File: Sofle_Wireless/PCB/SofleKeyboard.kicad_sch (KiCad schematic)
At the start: 121 parts, among them J1 Conn_01x05, SW1 SW1, SW10 SW10, SW11 SW11, SW12 SW12, SW13 SW13, SW14 SW14, SW15 SW15, SW16 SW16, SW17 SW17, SW18 SW18, SW19 SW19, SW2 SW2, SW20 SW20, SW21 SW21, SW22 SW22, SW23 SW23, SW24 SW24, SW25 SW19, SW26 SW26, SW27 SW27, SW28 SW28, SW29 SW29, SW3 SW3, SW30 SW30, SW4 SW4, SW5 SW5, SW6 SW6, SW7 SW7, SW8 SW8, SW9 SW9, U1 NICE!NANO

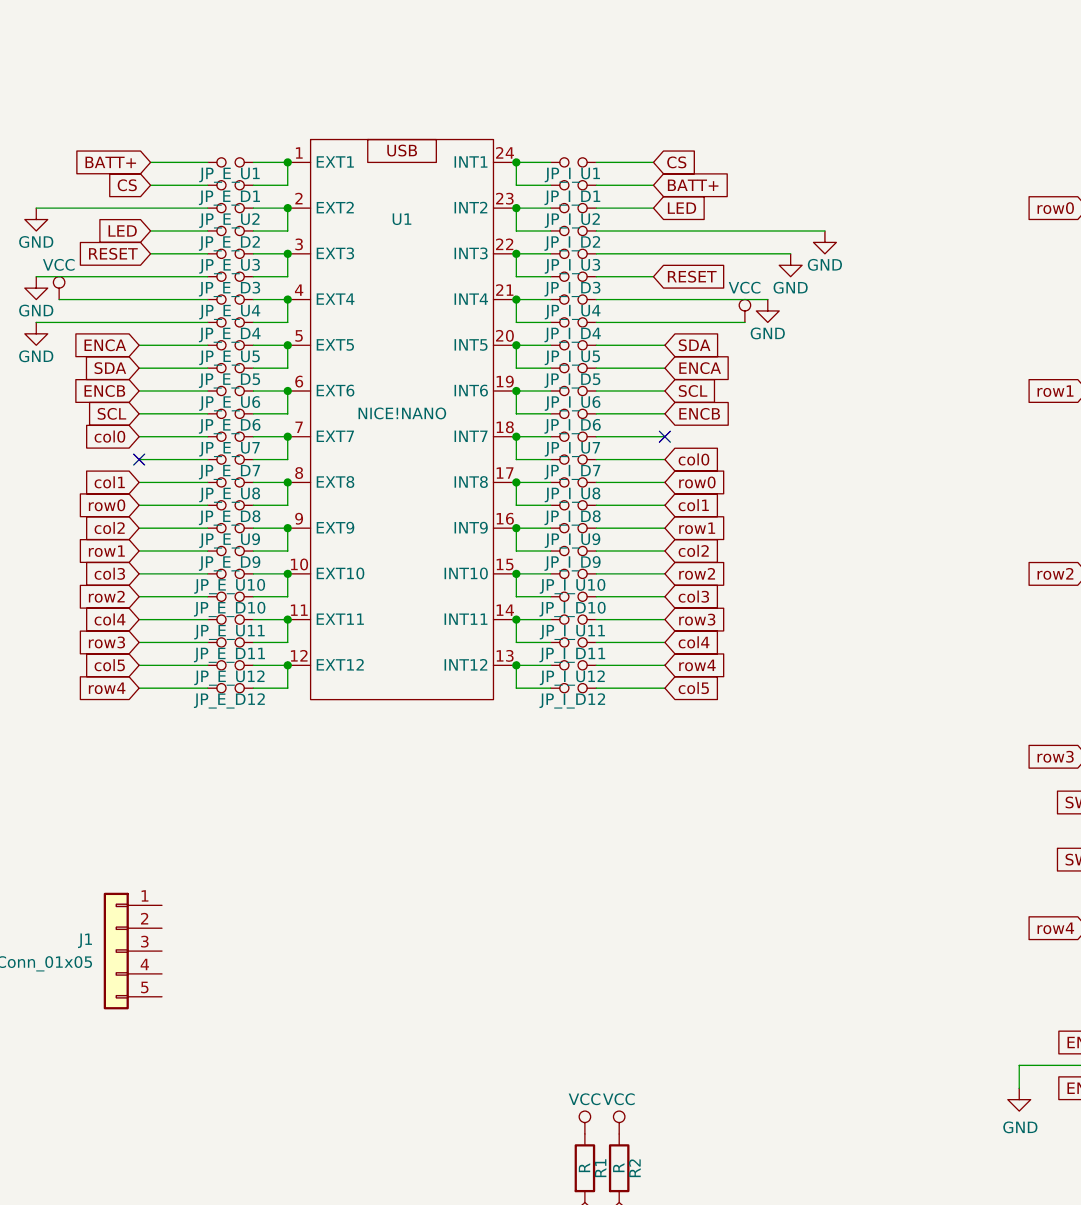
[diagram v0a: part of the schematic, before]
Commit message: Work on Footprints, PCB and schematic
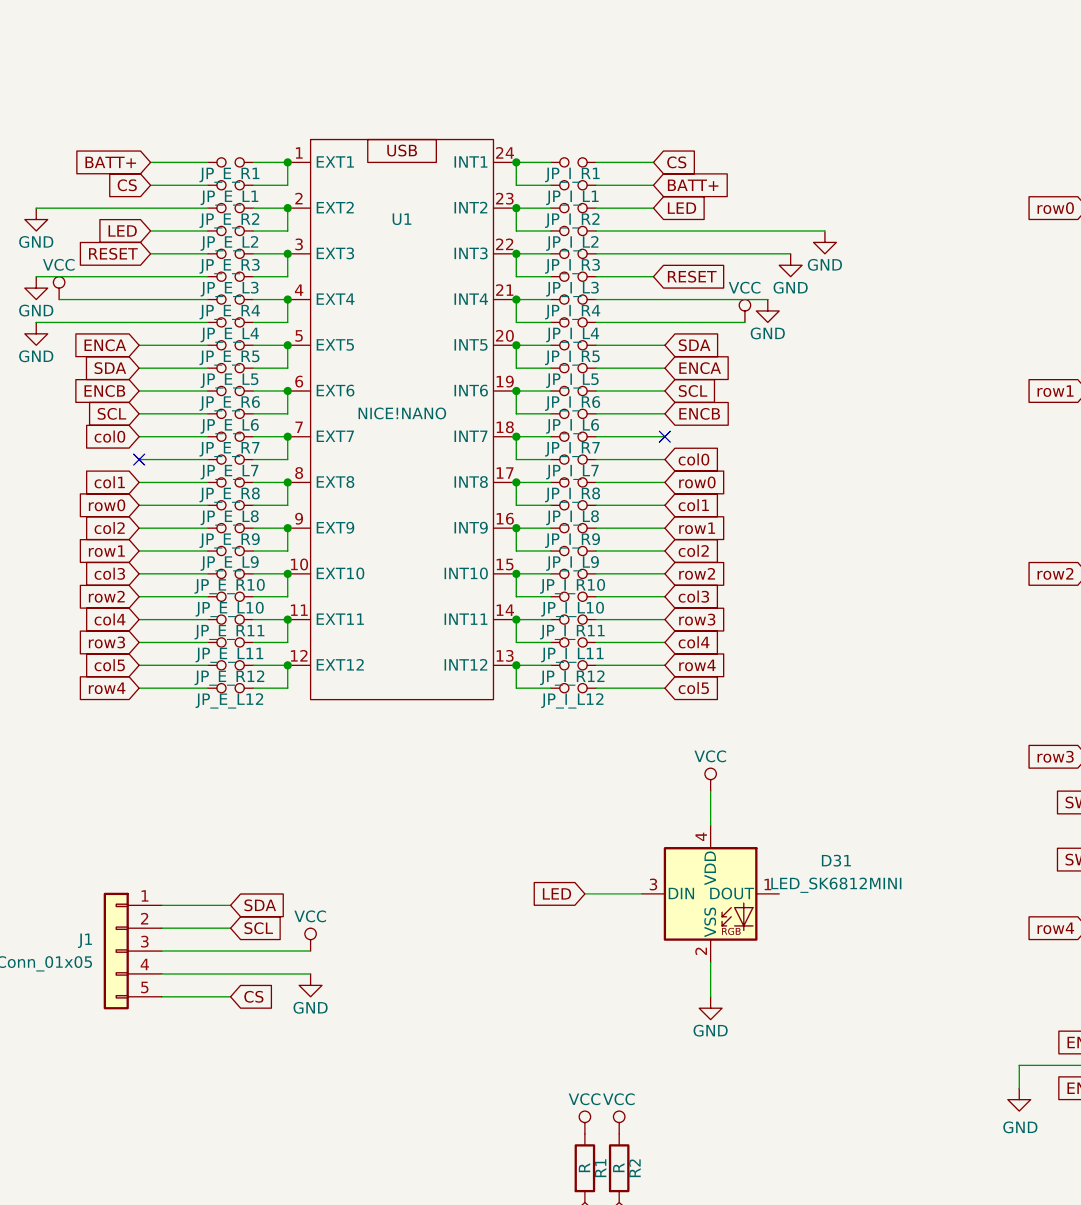
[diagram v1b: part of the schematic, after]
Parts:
- removed JP_E_D10, JP_E_D11, JP_E_D12, JP_E_D2, JP_E_D3, JP_E_D4, JP_E_D5, JP_E_D6, JP_E_D7, JP_E_D8, JP_E_D9, JP_E_U10, JP_E_U11, JP_E_U12, JP_E_U2, JP_E_U3, JP_E_U4, JP_E_U5, JP_E_U6, JP_E_U7, JP_E_U8, JP_E_U9, JP_I_D10, JP_I_D11, JP_I_D12, JP_I_D2, JP_I_D3, JP_I_D4, JP_I_D5, JP_I_D6, JP_I_D7, JP_I_D8, JP_I_D9, JP_I_U10, JP_I_U11, JP_I_U12, JP_I_U2, JP_I_U3, JP_I_U4, JP_I_U5, JP_I_U6, JP_I_U7, JP_I_U8, JP_I_U9: Jumper_NO_Small, Jumper:SolderJumper-2_P1.3mm_Open_Pad1.0x1.5mm, symbol SofleKeyboard-rescue:Jumper_NO_Small-Device
- added D31: LED_SK6812MINI, ScottoKeebs_Components:LED_SK6812MINI, symbol ScottoKeebs:LED_SK6812MINI
- added JP_E_L10, JP_E_L11, JP_E_L12, JP_E_L2, JP_E_L3, JP_E_L4, JP_E_L5, JP_E_L6, JP_E_L7, JP_E_L8, JP_E_L9: Jumper_NO_Small, Mechanical_Switches:SolderJumper-2_P1.3mm_Open_TrianglePad1.0x1.5mm_E, symbol SofleKeyboard-rescue:Jumper_NO_Small-Device
- added JP_E_R10, JP_E_R11, JP_E_R12, JP_E_R2, JP_E_R3, JP_E_R4, JP_E_R5, JP_E_R6, JP_E_R7, JP_E_R8, JP_E_R9: Jumper_NO_Small, Mechanical_Switches:SolderJumper-2_P1.3mm_Open_TrianglePad1.0x1.5mm_E_Reverse, symbol SofleKeyboard-rescue:Jumper_NO_Small-Device
- added JP_I_L10, JP_I_L11, JP_I_L12, JP_I_L2, JP_I_L3, JP_I_L4, JP_I_L5, JP_I_L6, JP_I_L7, JP_I_L8, JP_I_L9: Jumper_NO_Small, Mechanical_Switches:SolderJumper-2_P1.3mm_Open_TrianglePad1.0x1.5mm_I, symbol SofleKeyboard-rescue:Jumper_NO_Small-Device
- added JP_I_R10, JP_I_R11, JP_I_R12, JP_I_R2, JP_I_R3, JP_I_R4, JP_I_R5, JP_I_R6, JP_I_R7, JP_I_R8, JP_I_R9: Jumper_NO_Small, Mechanical_Switches:SolderJumper-2_P1.3mm_Open_TrianglePad1.0x1.5mm_I_Reverse, symbol SofleKeyboard-rescue:Jumper_NO_Small-Device
- EC1: footprint Rotary_Encoder:RotaryEncoder_Alps_EC12E-Switch_Vertical_H20mm -> Mechanical_Switches:RotaryEncoder_Alps_EC12E-Switch_Vertical_H20mm
- JP_E_L1: renamed from JP_E_D1; footprint Jumper:SolderJumper-2_P1.3mm_Open_Pad1.0x1.5mm -> Mechanical_Switches:SolderJumper-2_P1.3mm_Open_TrianglePad1.0x1.5mm_E
- JP_E_R1: renamed from JP_E_U1; footprint Jumper:SolderJumper-2_P1.3mm_Open_Pad1.0x1.5mm -> Mechanical_Switches:SolderJumper-2_P1.3mm_Open_TrianglePad1.0x1.5mm_E_Reverse
- JP_I_L1: renamed from JP_I_D1; footprint Jumper:SolderJumper-2_P1.3mm_Open_Pad1.0x1.5mm -> Mechanical_Switches:SolderJumper-2_P1.3mm_Open_TrianglePad1.0x1.5mm_I
- JP_I_R1: renamed from JP_I_U1; footprint Jumper:SolderJumper-2_P1.3mm_Open_Pad1.0x1.5mm -> Mechanical_Switches:SolderJumper-2_P1.3mm_Open_TrianglePad1.0x1.5mm_I_Reverse
- R1, R2: footprint kbd:R -> Resistor_SMD:R_0805_2012Metric_Pad1.20x1.40mm_HandSolder
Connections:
- net CS: now also J1.5 (Pin_5)
- net ENCA: now also JP_E_R5.1, JP_I_L5.2
- net ENCB: now also JP_E_R6.1, JP_I_L6.2
- net GND: now also J1.4 (Pin_4), D31.2 (VSS), JP_E_L3.1, JP_E_L4.1, JP_E_R2.1, JP_I_L2.2, JP_I_R3.2, JP_I_R4.2
- net LED: now also D31.3 (DIN), JP_E_L2.1, JP_I_R2.2
- net RESET: now also JP_E_R3.1, JP_I_L3.2
- net SCL: now also J1.2 (Pin_2), JP_E_L6.1, JP_I_R6.2
- net SDA: now also J1.1 (Pin_1), JP_E_L5.1, JP_I_R5.2
- net SW25A: now also JP_E_R12.1, JP_I_L12.2
- net VCC: now also J1.3 (Pin_3), D31.4 (VDD), JP_E_R4.1, JP_I_L4.2
- net col0: now also JP_E_R7.1, JP_I_L7.2
- net col1: now also JP_E_R8.1, JP_I_L8.2
- net col2: now also JP_E_R9.1, JP_I_L9.2
- net col3: now also JP_E_R10.1, JP_I_L10.2
- net col4: now also JP_E_R11.1, JP_I_L11.2
- net row0: now also JP_E_L8.1, JP_I_R8.2
- net row1: now also JP_E_L9.1, JP_I_R9.2
- net row2: now also JP_E_L10.1, JP_I_R10.2
- net row3: now also JP_E_L11.1, JP_I_R11.2
- net row4: now also JP_E_L12.1, JP_I_R12.2
- net at U1.20 (INT5): now also JP_I_L5.1, JP_I_R5.1
- net at U1.3 (EXT3): now also JP_E_L3.2, JP_E_R3.2
- net at U1.16 (INT9): now also JP_I_L9.1, JP_I_R9.1
- net at U1.6 (EXT6): now also JP_E_L6.2, JP_E_R6.2
- net at U1.8 (EXT8): now also JP_E_L8.2, JP_E_R8.2
- net at U1.17 (INT8): now also JP_I_L8.1, JP_I_R8.1
- net at U1.13 (INT12): now also JP_I_L12.1, JP_I_R12.1
- net at U1.9 (EXT9): now also JP_E_L9.2, JP_E_R9.2
- net at U1.7 (EXT7): now also JP_E_L7.2, JP_E_R7.2
- net at U1.22 (INT3): now also JP_I_L3.1, JP_I_R3.1
- net at U1.12 (EXT12): now also JP_E_L12.2, JP_E_R12.2
- net at U1.14 (INT11): now also JP_I_L11.1, JP_I_R11.1
- net at U1.10 (EXT10): now also JP_E_L10.2, JP_E_R10.2
- net at U1.18 (INT7): now also JP_I_L7.1, JP_I_R7.1
- net at U1.19 (INT6): now also JP_I_L6.1, JP_I_R6.1
- net at U1.11 (EXT11): now also JP_E_L11.2, JP_E_R11.2
- net at U1.15 (INT10): now also JP_I_L10.1, JP_I_R10.1
- net at U1.2 (EXT2): now also JP_E_L2.2, JP_E_R2.2
- net at U1.21 (INT4): now also JP_I_L4.1, JP_I_R4.1
- net at U1.23 (INT2): now also JP_I_L2.1, JP_I_R2.1
- net at U1.4 (EXT4): now also JP_E_L4.2, JP_E_R4.2
- net at U1.5 (EXT5): now also JP_E_L5.2, JP_E_R5.2

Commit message: Work on traces
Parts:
- added D32, D33, D34, D35, D36, D37, D38, D39, D40, D41: LED_SK6812MINI, RGB_LED:SK6812_Mini-E_DualSide, symbol RGB_LED:SK6812_Mini-E
- added JP_ENC_LA1, JP_ENC_LB1, JP_LCD_L1, JP_LCD_L2, JP_LCD_L4, JP_LCD_L5: Jumper_NO_Small, Mechanical_Switches:SolderJumper-2_P1.3mm_Open_TrianglePad1.0x1.5mm_E, symbol SofleKeyboard-rescue:Jumper_NO_Small-Device
- added JP_ENC_RA1, JP_ENC_RB1, JP_LCD_R1, JP_LCD_R2, JP_LCD_R4, JP_LCD_R5: Jumper_NO_Small, Mechanical_Switches:SolderJumper-2_P1.3mm_Open_TrianglePad1.0x1.5mm_E_Reverse, symbol SofleKeyboard-rescue:Jumper_NO_Small-Device
- D31: footprint ScottoKeebs_Components:LED_SK6812MINI -> RGB_LED:SK6812_Mini-E_DualSide; symbol ScottoKeebs:LED_SK6812MINI -> RGB_LED:SK6812_Mini-E
- R1, R2: footprint Resistor_SMD:R_0805_2012Metric_Pad1.20x1.40mm_HandSolder -> Mechanical_Switches:R_0805_2012Metric_Pad1.20x1.40mm_HandSolder_dualside
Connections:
- net CS: now also JP_LCD_L2.2, JP_LCD_R5.2; no longer J1.5 (Pin_5)
- net ENCA: now also JP_ENC_LB1.1, JP_ENC_RA1.1; no longer EC1.A
- net ENCB: now also JP_ENC_LA1.1, JP_ENC_RB1.1; no longer EC1.B
- net GND: now also D31.3 (GND), D32.3 (GND), D33.3 (GND), D34.3 (GND), D35.3 (GND), D36.3 (GND), D37.3 (GND), D38.3 (GND), D39.3 (GND), D40.3 (GND), D41.3 (GND), JP_LCD_L1.2, JP_LCD_R4.2; no longer D31.2 (VSS), J1.4 (Pin_4)
- net LED: now also D31.4 (DIN); no longer D31.3 (DIN)
- net SCL: now also JP_LCD_L4.2, JP_LCD_R2.2; no longer J1.2 (Pin_2)
- net SDA: now also JP_LCD_L5.2, JP_LCD_R1.2; no longer J1.1 (Pin_1)
- net VCC: now also D31.1 (VDD), D32.1 (VDD), D33.1 (VDD), D34.1 (VDD), D35.1 (VDD), D36.1 (VDD), D37.1 (VDD), D38.1 (VDD), D39.1 (VDD), D40.1 (VDD), D41.1 (VDD); no longer D31.4 (VDD)
- net SW25A renamed col5
- net SW25B: no longer names the net of D25.2 (A), EC1.S2, SW25.2
- new net: EC1.A, JP_ENC_LA1.2, JP_ENC_RA1.2
- new net: EC1.B, JP_ENC_LB1.2, JP_ENC_RB1.2
- new net: D40.2 (DOUT), D41.4 (DIN)
- new net: D34.2 (DOUT), D35.4 (DIN)
- new net: D33.2 (DOUT), D34.4 (DIN)
- new net: D31.2 (DOUT), D32.4 (DIN)
- new net: D32.2 (DOUT), D33.4 (DIN)
- new net: D38.2 (DOUT), D39.4 (DIN)
- new net: D37.2 (DOUT), D38.4 (DIN)
- new net: J1.2 (Pin_2), JP_LCD_L1.1, JP_LCD_R2.1
- new net: J1.5 (Pin_5), JP_LCD_L5.1, JP_LCD_R5.1
- new net: J1.1 (Pin_1), JP_LCD_L2.1, JP_LCD_R1.1
- new net: D39.2 (DOUT), D40.4 (DIN)
- new net: J1.4 (Pin_4), JP_LCD_L4.1, JP_LCD_R4.1
- new net: D35.2 (DOUT), D36.4 (DIN)
- new net: D36.2 (DOUT), D37.4 (DIN)
- no-connect marks 2 -> 3
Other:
- moved on the sheet: D1, D10, D11, D12, D13, D14, D15, D16, D17, D18, D19, D2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

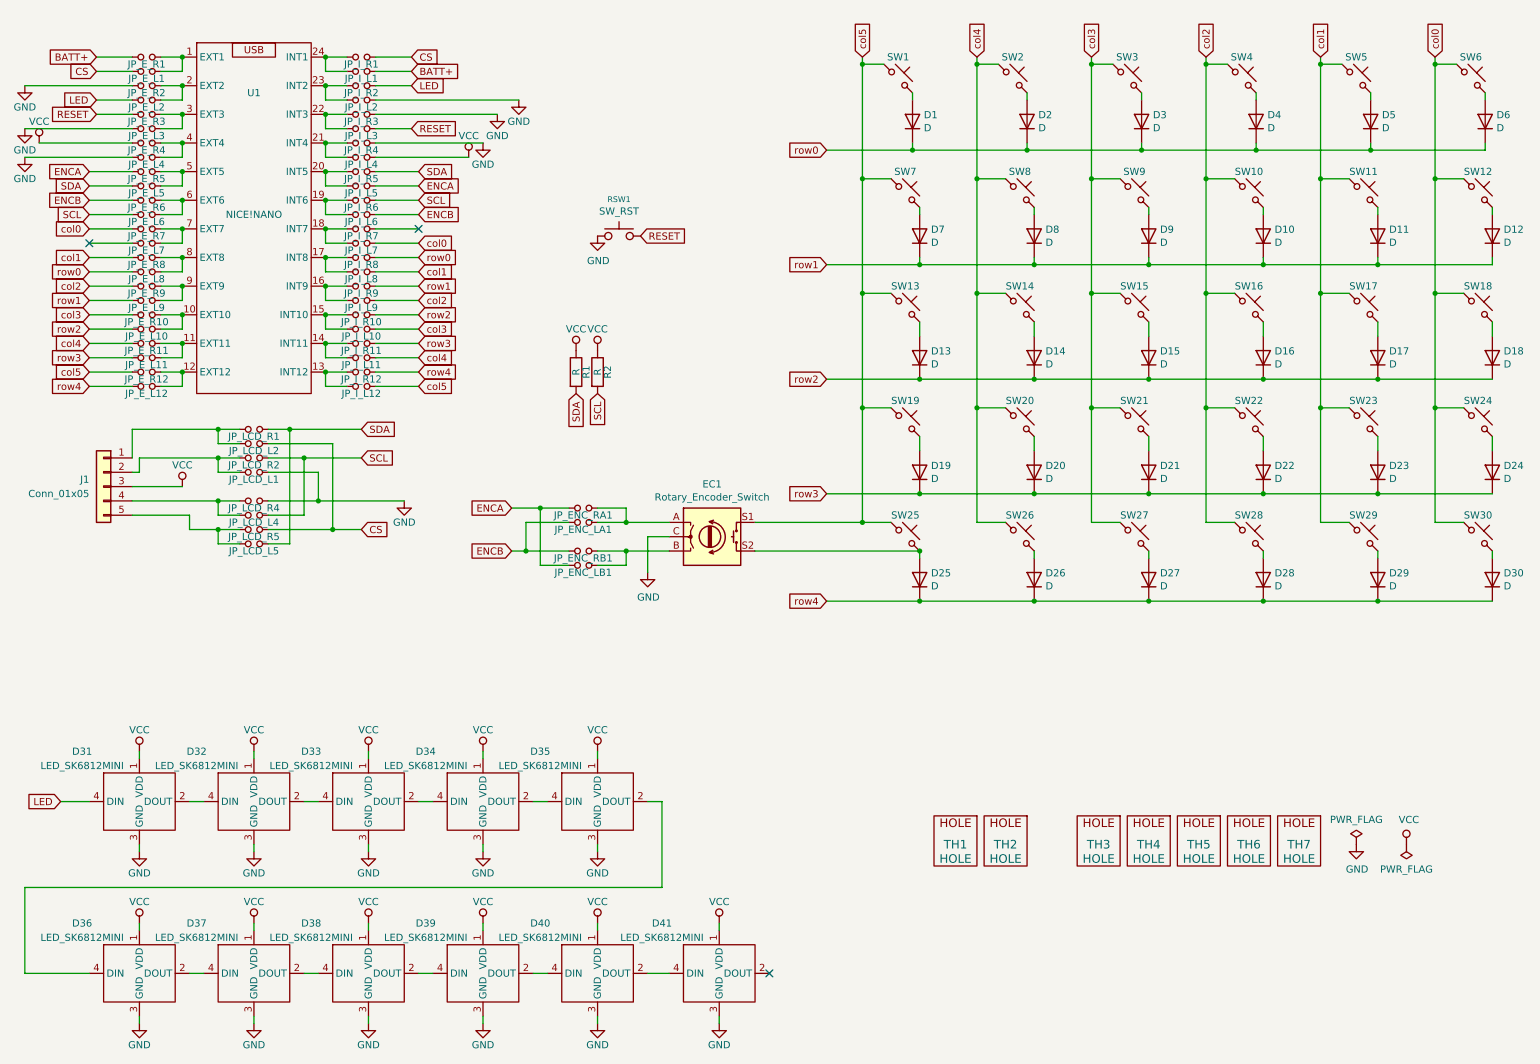
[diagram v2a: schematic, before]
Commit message: Work on part placement and trace routing.
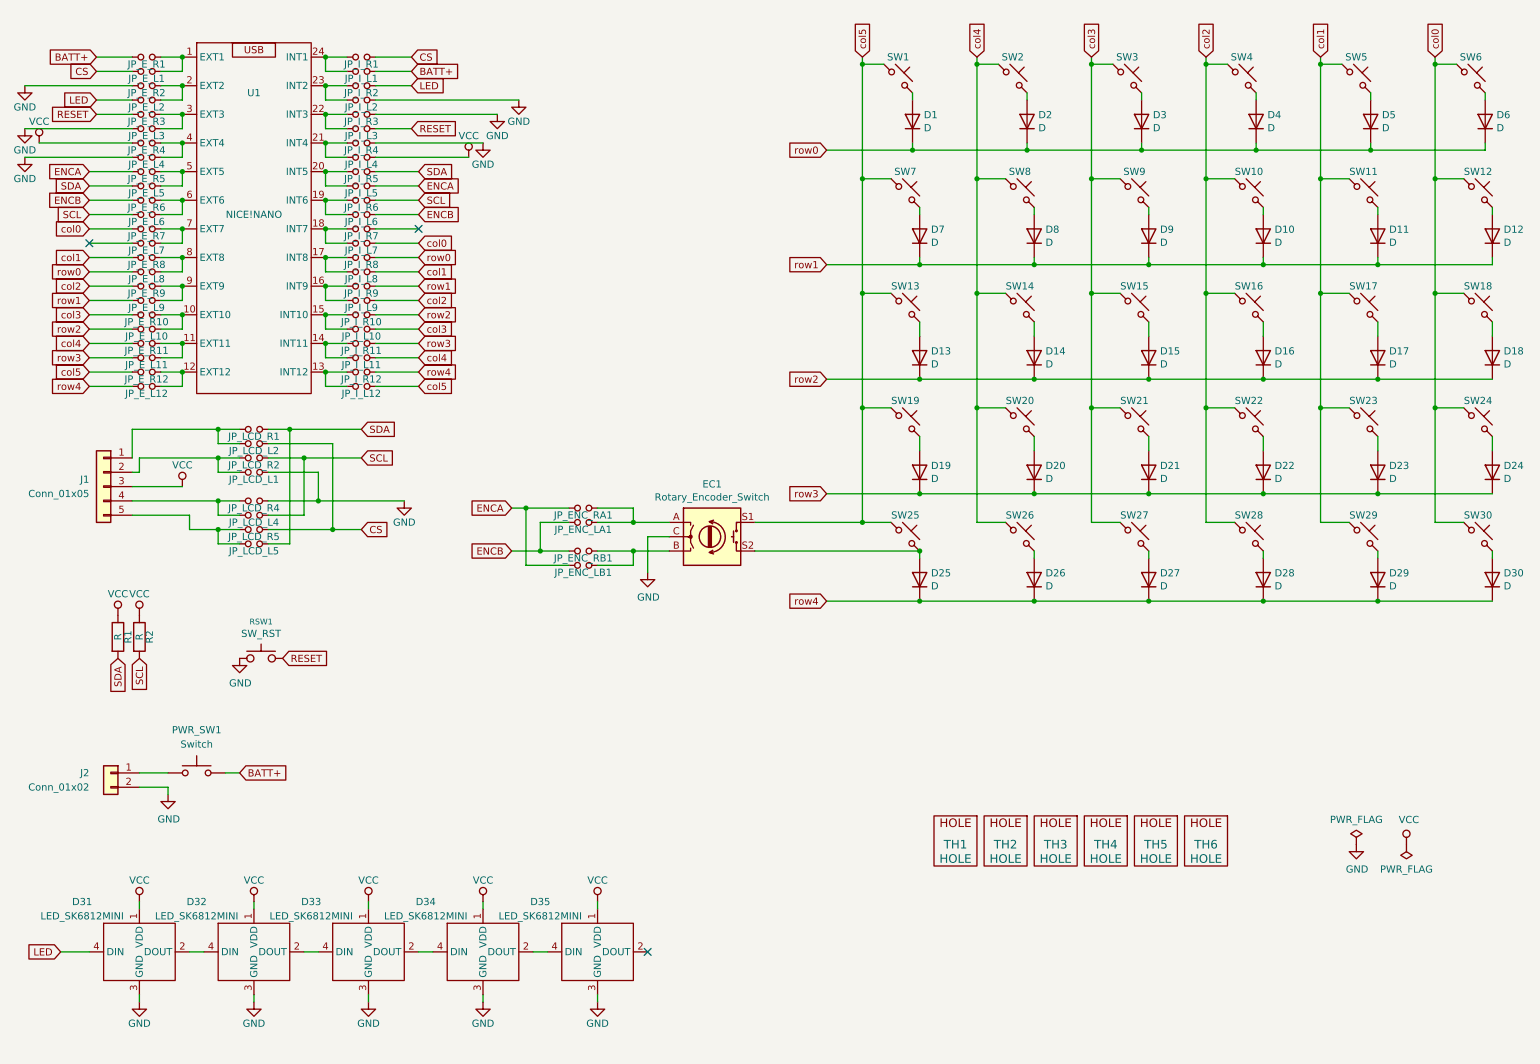
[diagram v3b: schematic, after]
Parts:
- removed D36, D37, D38, D39, D40, D41: LED_SK6812MINI, RGB_LED:SK6812_Mini-E_DualSide, symbol RGB_LED:SK6812_Mini-E
- removed TH1, TH2: HOLE, MountingHole:MountingHole_2.2mm_M2, symbol SofleKeyboard-rescue:HOLE-Lily58-cache-Lily58_Pro-rescue
- added J2: Conn_01x02, Mechanical_Switches:JST_PH_S2B-PH-SM4-TB_1x02-1MP_P2.00mm_Horizontal_DualSide, symbol Connector_Generic:Conn_01x02
- added PWR_SW1: Switch, Mechanical_Switches:SLW-1276864-4A-D, symbol ScottoKeebs:Placeholder_Switch
- added TH6: HOLE, MountingHole:MountingHole_2.2mm_M2, symbol SofleKeyboard-rescue:HOLE-Lily58-cache-Lily58_Pro-rescue
- renumbered TH3 to TH1, TH4 to TH2, TH5 to TH3, TH6 to TH4, TH7 to TH5
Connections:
- net BATT+: now also PWR_SW1.2
- net ENCA: now also JP_ENC_LB1.2, JP_ENC_RA1.2; no longer JP_ENC_LB1.1, JP_ENC_RA1.1
- net ENCB: now also JP_ENC_LA1.2, JP_ENC_RB1.2; no longer JP_ENC_LA1.1, JP_ENC_RB1.1
- net GND: now also J2.2 (Pin_2)
- new net: EC1.A, JP_ENC_LA1.1, JP_ENC_RA1.1
- new net: EC1.B, JP_ENC_LB1.1, JP_ENC_RB1.1
- new net: J2.1 (Pin_1), PWR_SW1.1
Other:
- moved on the sheet: D31, D32, D33, D34, D35, R1, R2, RSW1, TH1, TH2, TH3, TH4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

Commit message: Added BOM
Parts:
- RSW1: footprint kbd:ResetSW -> Mechanical_Switches:ResetSW_DualSide
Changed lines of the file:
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@@
       (effects (font (size 1.27 1.27)))
     )
-    (property "Footprint" "kbd:ResetSW" (at 58.42 127 0)
+    (property "Footprint" "Mechanical_Switches:ResetSW_DualSide" (at 58.42 127 0)
       (effects (font (size 1.27 1.27)) hide)
     )
